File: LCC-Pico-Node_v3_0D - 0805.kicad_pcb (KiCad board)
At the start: 4 copper layers, 100 x 82 mm, 89 parts, among them IC1 TPS54228DR, IC2 MCP2518FD, IC3 MCP2562FD, IC5 256Kb, IC6 TPS54228DR, J1 RJ45, J12 Power Sel, J15 Analog I/O, J16 NVM Power Sel, J2 RJ45, J20 Barrel Jack, J21 I/O - 1, J24 Ext. Reset, J27 MasterPower, J3 LCC Pwr Sel, J4 I/O - 2, J5 External Power, J6 Power Sel, J7 External Power, Q1 DMG2305UX-7, SW1 button, SW2 button, SW3 button, Y1 ABM-40MHZ

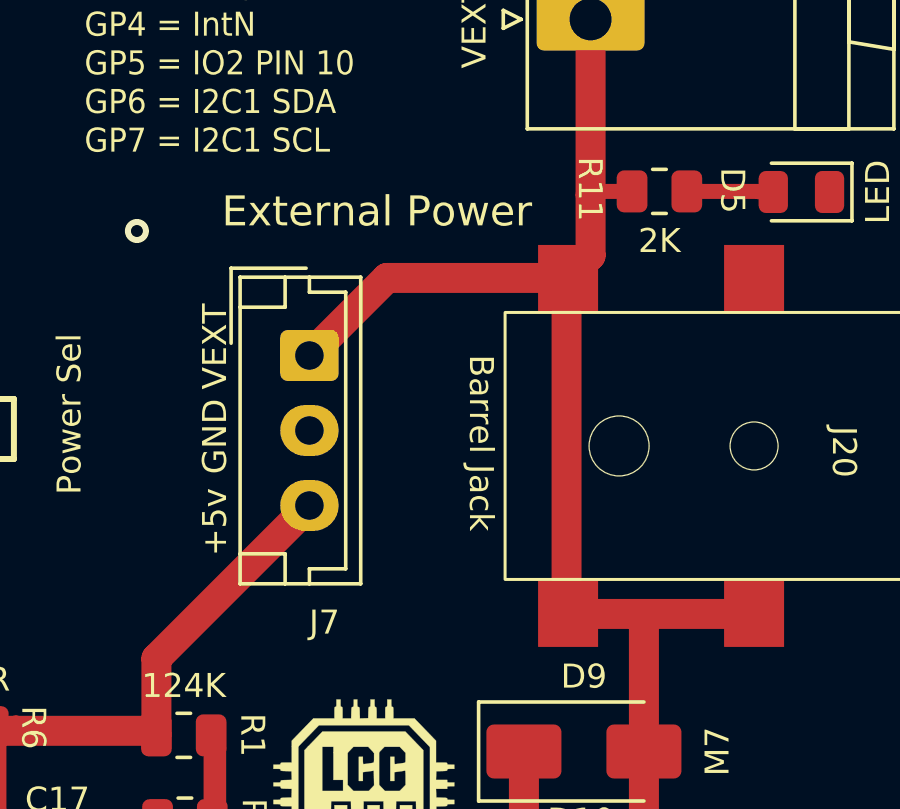
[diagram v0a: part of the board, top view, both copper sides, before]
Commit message: barrel jack footprint fix
bad footprint replaced
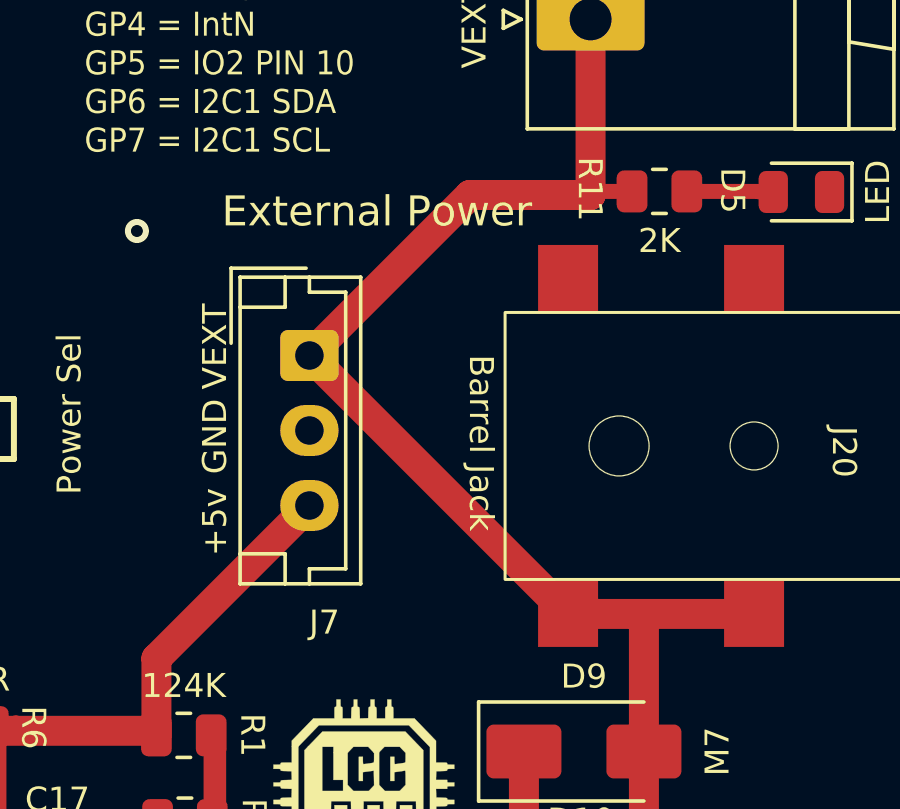
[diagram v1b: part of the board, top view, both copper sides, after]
